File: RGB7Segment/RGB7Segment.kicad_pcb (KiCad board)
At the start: 2 copper layers, 34 x 31.5 mm, 14 parts, among them J1 Conn_01x04_Female, J2 Conn_01x04_Female

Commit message: Slotted/Cut Design Uploaded. Waiting on COnfirmation of Operation
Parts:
- removed D3, D4: SK6812-E, Library:12-23C
- removed J2: Conn_01x04_Female, Connector_PinHeader_2.54mm:PinHeader_1x04_P2.54mm_Vertical
- removed R1, R2: 0, Resistor_SMD:R_0402_1005Metric
- added A2: SK6812-E, Library:12-23C, F.Cu at (192.7, 76.5)
- added B2: SK6812-E, Library:12-23C, F.Cu at (196.7, 77.7)
- added C2: 0.470u, Capacitor_SMD:C_0402_1005Metric, F.Cu at (187.5, 77.0)
- added C3: 0.1u, Capacitor_SMD:C_0402_1005Metric, F.Cu at (181.2, 78.8)
- added C4: 0.1u, Capacitor_SMD:C_0402_1005Metric, F.Cu at (181.5, 85.0)
- added C5: SK6812-E, Library:12-23C, F.Cu at (196.7, 83.7)
- added C8: 0.1u, Capacitor_SMD:C_0402_1005Metric, F.Cu at (194.2, 79.0)
- added C9: 0.1u, Capacitor_SMD:C_0402_1005Metric, F.Cu at (193.9, 85.2)
- added E2: SK6812-E, Library:12-23C, F.Cu at (191.4, 86.3)
- added F2: SK6812-E, Library:12-23C, F.Cu at (191.4, 80.3)
- added G2: SK6812-E, Library:12-23C, F.Cu at (192.7, 82.5)
- A1, D1: footprint Library:4960_ADA -> Library:12-23C
- B1: footprint Library:4960_Test2 -> Library:12-23C
- C1, G1: footprint Library:4960_Test4 -> Library:12-23C
- E1: footprint Library:4960_Test3 -> Library:12-23C
- F1: footprint Library:4960_Test1 -> Library:12-23C
- moved C1 27.0 mm to (184.0, 83.7), turned to -90 degrees
- moved D2 26.1 mm to (195.3, 87.5), turned to 180 degrees
- moved B1 25.1 mm to (184.0, 77.7), turned to -90 degrees
- moved D1 24.1 mm to (182.6, 87.5), turned to 180 degrees
- moved G1 24.0 mm to (180.0, 82.5), turned to 0 degrees
- moved A1 22.1 mm to (180.0, 76.5)
- moved E1 21.0 mm to (178.7, 86.3), turned to 90 degrees
- moved F1 19.0 mm to (178.7, 80.3), turned to 90 degrees
- moved J1 8.30 mm to (187.5, 80.0)
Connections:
- net +3V3 renamed VCC
- A1 pad 2: Net-(A1-Pad2) -> /F1
- A1 pad 4: Net-(R2-Pad2) -> /A1
- B1 pad 2: Net-(B1-Pad2) -> /A1
- B1 pad 4: Net-(A1-Pad2) -> /DIN
- C1 pad 2: /D1 -> /G1
- C1 pad 4: Net-(B1-Pad2) -> /C1
- D1 pad 2: Net-(D1-Pad2) -> /C1
- D2 pad 2: Net-(D2-Pad2) -> /C2
- D2 pad 4: Net-(D2-Pad4) -> /D2
- E1 pad 2: Net-(E1-Pad2) -> /D1
- E1 pad 4: Net-(D1-Pad2) -> /E1
- F1 pad 2: Net-(F1-Pad2) -> /E1
- F1 pad 4: Net-(E1-Pad2) -> /F1
- G1 pad 2: /D2 -> /E2
- G1 pad 4: Net-(F1-Pad2) -> /G1
- J1 pad 3: unconnected-(J1-Pad3) -> /DOUT
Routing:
- net VCC: track 130.3 -> 68.7 mm, vias 0 -> 4
- net Net-(E1-Pad2): track 21.2 -> 0.00 mm
- net /DIN: track 24.8 -> 5.04 mm
- net Net-(D2-Pad4): track 18.3 -> 0.00 mm
- net /E2: track 0.00 -> 16.1 mm
- net Net-(A1-Pad2): track 12.6 -> 0.00 mm
- net Net-(R2-Pad2): track 12.0 -> 0.00 mm
- net Net-(B1-Pad2): track 11.0 -> 0.00 mm
- net Net-(F1-Pad2): track 9.52 -> 0.00 mm
- net Net-(D2-Pad2): track 8.73 -> 0.00 mm
- net Net-(D1-Pad2): track 8.00 -> 0.00 mm
- net /DOUT: track 0.00 -> 7.65 mm, vias 0 -> 1
- net /G2: track 0.00 -> 7.44 mm, vias 0 -> 2
- net GND: track 13.8 -> 18.6 mm, vias 9 -> 19
- net /B2: track 0.00 -> 3.67 mm
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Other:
- board size 34 x 31.5 mm -> 21.8 x 14.5 mm

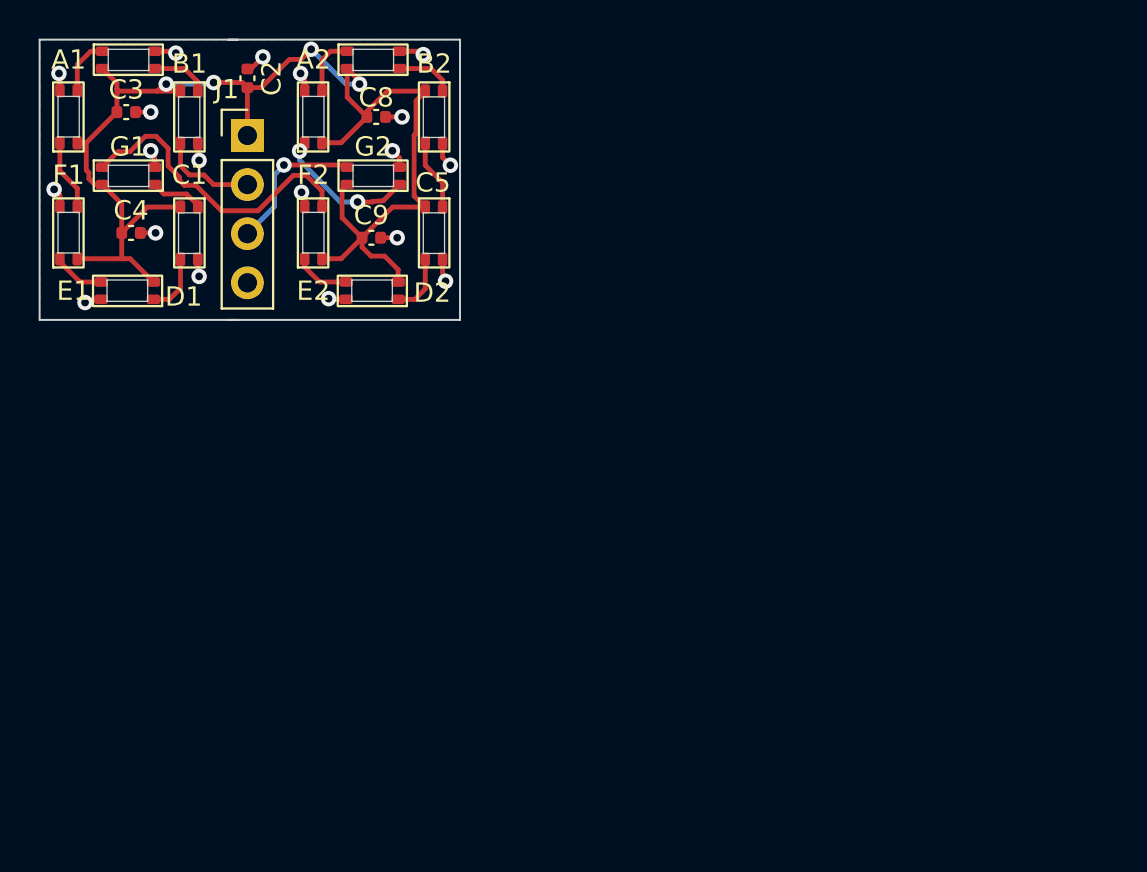
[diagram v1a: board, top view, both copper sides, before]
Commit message: Moving Design over to non cutout.
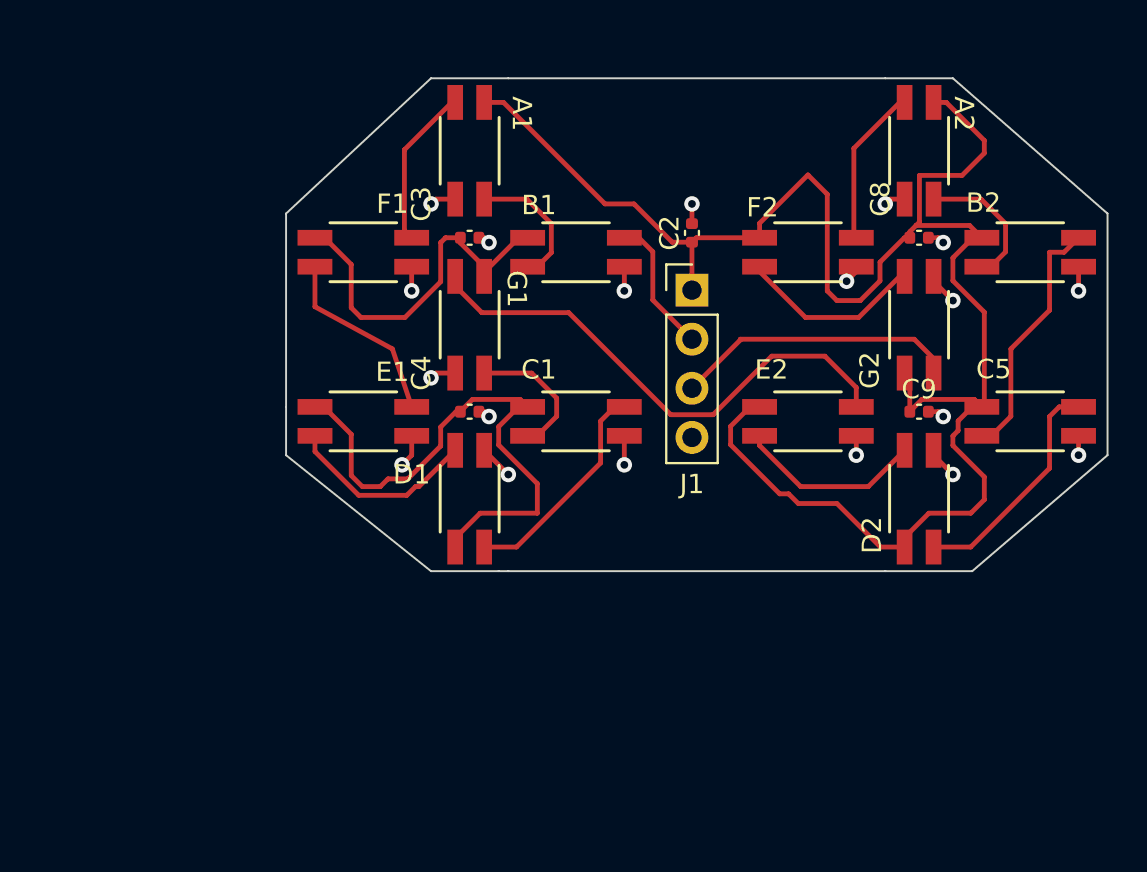
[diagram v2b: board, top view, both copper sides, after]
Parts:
- A1, A2, B1, B2, C1, C5, D1, D2, E1, E2, F1, F2, G1, G2: footprint Library:12-23C -> Library:4960_Test4
- moved C5 33.2 mm to (228.0, 94.7), turned to 0 degrees
- moved B2 32.4 mm to (228.0, 86.0), turned to 0 degrees
- moved G2 30.5 mm to (222.3, 89.8), turned to 90 degrees
- moved A2 29.9 mm to (222.3, 80.8), turned to -90 degrees
- moved C9 29.7 mm to (222.3, 94.3)
- moved D2 29.2 mm to (222.3, 98.8), turned to 90 degrees
- moved C8 28.8 mm to (222.3, 85.3)
- moved E2 26.5 mm to (216.5, 94.8), turned to 0 degrees
- moved F2 25.8 mm to (216.5, 86.0), turned to 0 degrees
- moved C2 24.4 mm to (210.5, 85.0)
- moved J1 24.4 mm to (210.5, 88.0)
- moved C1 23.3 mm to (204.5, 94.8), turned to 0 degrees
- moved B1 22.1 mm to (204.5, 86.0), turned to 0 degrees
- moved G1 20.3 mm to (199.0, 89.8), turned to -90 degrees
- moved D1 19.8 mm to (199.0, 98.8), turned to 90 degrees
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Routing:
- net VCC: track 68.7 -> 142.6 mm, vias 4 -> 0
- net /E2: track 16.1 -> 26.9 mm
- net /B2: track 3.67 -> 13.1 mm
- net /C2: track 3.16 -> 12.1 mm
- net /C1: track 3.14 -> 11.5 mm
- net /D1: track 2.73 -> 9.97 mm
- net /DOUT: track 7.65 -> 14.7 mm, vias 1 -> 0
- net /D2: track 2.88 -> 9.66 mm
- net /E1: track 3.67 -> 9.79 mm
- net /F1: track 2.93 -> 8.35 mm
- net /F2: track 3.08 -> 8.29 mm
- net GND: track 18.6 -> 22.8 mm
- net /A2: track 3.05 -> 7.26 mm
- net /G1: track 2.99 -> 7.15 mm
- net /A1: track 3.00 -> 7.03 mm
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- removed copper zone on B.Cu, net GND
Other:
- board size 21.8 x 14.5 mm -> 42.5 x 25.5 mm

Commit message: Cleaning up PCB, and minor cleanup.
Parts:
- added J2: Conn_01x02_Socket, Connector_PinHeader_2.54mm:PinHeader_1x02_P2.54mm_Vertical, F.Cu at (207.2, 100.0)
- J1: value Conn_01x04_Female -> Conn_01x02_Socket; footprint Connector_PinHeader_2.54mm:PinHeader_1x04_P2.54mm_Vertical -> Connector_PinHeader_2.54mm:PinHeader_1x02_P2.54mm_Vertical
- moved J1 9.07 mm to (207.2, 79.5), turned to 90 degrees
- moved A2 4.00 mm to (218.3, 80.8)
- moved B2 4.00 mm to (224.0, 86.0)
- moved C5 4.00 mm to (224.0, 94.7)
- moved C8 4.00 mm to (218.3, 85.3)
- moved C9 4.00 mm to (218.3, 94.3)
- moved D2 4.00 mm to (218.3, 98.8)
- moved E2 4.00 mm to (212.5, 94.8)
- moved F2 4.00 mm to (212.5, 86.0)
- moved G2 4.00 mm to (218.3, 89.8)
- moved C2 3.61 mm to (208.5, 82.0), turned to 180 degrees
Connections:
- J1 pad 1: VCC -> GND
- J1 pad 2: /DIN -> VCC
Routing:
- net VCC: track 142.6 -> 3.70 mm
- net /E2: track 26.9 -> 0.00 mm
- net GND: track 22.8 -> 1.02 mm, vias 19 -> 1
- net /DOUT: track 14.7 -> 0.00 mm
- net /B2: track 13.1 -> 0.00 mm
- net /C2: track 12.1 -> 0.00 mm
- net /C1: track 11.5 -> 0.00 mm
- net /D1: track 9.97 -> 0.00 mm
- net /E1: track 9.79 -> 0.00 mm
- net /D2: track 9.66 -> 0.00 mm
- net /G2: track 9.62 -> 0.00 mm
- net /F1: track 8.35 -> 0.00 mm
- net /F2: track 8.29 -> 0.00 mm
- net /A2: track 7.26 -> 0.00 mm
- net /G1: track 7.15 -> 0.00 mm
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- added copper zone on B.Cu, net GND
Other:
- board size 42.5 x 25.5 mm -> 38.5 x 25.5 mm

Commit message: Adding New Models,
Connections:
- A1 pad 2: /F1 -> unconnected-(A1-DOUT-Pad2)
- A1 pad 4: /A1 -> unconnected-(A1-DIN-Pad4)
- A2 pad 2: /F2 -> unconnected-(A2-DOUT-Pad2)
- A2 pad 4: /A2 -> unconnected-(A2-DIN-Pad4)
- B1 pad 2: /A1 -> unconnected-(B1-DOUT-Pad2)
- B1 pad 4: /DIN -> unconnected-(B1-DIN-Pad4)
- B2 pad 2: /A2 -> unconnected-(B2-DOUT-Pad2)
- B2 pad 4: /B2 -> unconnected-(B2-DIN-Pad4)
- C1 pad 2: /G1 -> unconnected-(C1-DOUT-Pad2)
- C1 pad 4: /C1 -> /DIN
- C5 pad 2: /B2 -> unconnected-(C5-DOUT-Pad2)
- C5 pad 4: /C2 -> unconnected-(C5-DIN-Pad4)
- D1 pad 2: /C1 -> unconnected-(D1-DOUT-Pad2)
- D1 pad 4: /D1 -> unconnected-(D1-DIN-Pad4)
- D2 pad 2: /C2 -> unconnected-(D2-DOUT-Pad2)
- D2 pad 4: /D2 -> unconnected-(D2-DIN-Pad4)
- E1 pad 2: /D1 -> unconnected-(E1-DOUT-Pad2)
- E1 pad 4: /E1 -> unconnected-(E1-DIN-Pad4)
- E2 pad 2: /D2 -> /DOUT
- E2 pad 4: /E2 -> unconnected-(E2-DIN-Pad4)
- F1 pad 2: /E1 -> unconnected-(F1-DOUT-Pad2)
- F1 pad 4: /F1 -> unconnected-(F1-DIN-Pad4)
- F2 pad 2: /G2 -> unconnected-(F2-DOUT-Pad2)
- F2 pad 4: /F2 -> unconnected-(F2-DIN-Pad4)
- G1 pad 2: /E2 -> unconnected-(G1-DOUT-Pad2)
- G1 pad 4: /G1 -> unconnected-(G1-DIN-Pad4)
- G2 pad 2: /DOUT -> unconnected-(G2-DOUT-Pad2)
- G2 pad 4: /G2 -> unconnected-(G2-DIN-Pad4)
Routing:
- net VCC: track 3.70 -> 0.88 mm
- net GND: track 1.02 -> 0.00 mm, vias 1 -> 0

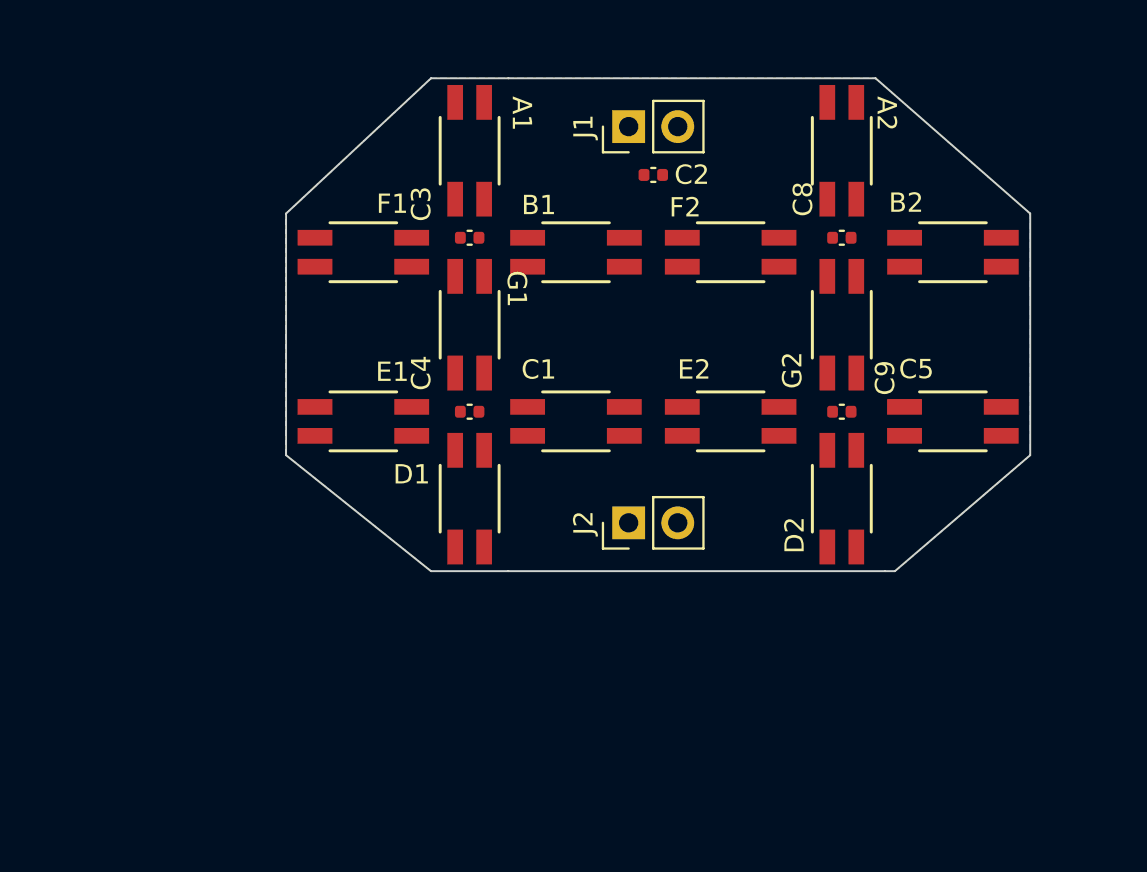
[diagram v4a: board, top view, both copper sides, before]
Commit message: Smaller Size first pass layout
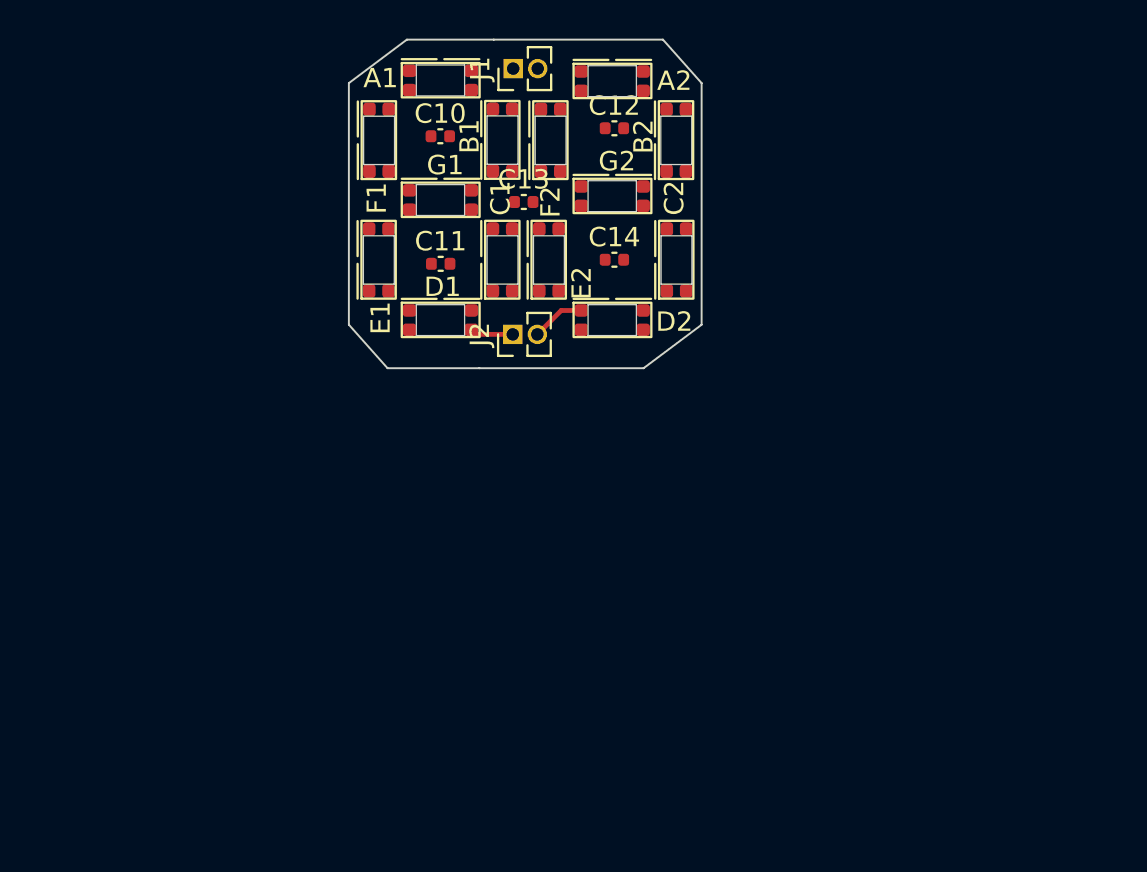
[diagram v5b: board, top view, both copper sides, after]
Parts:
- removed C3, C4, C8, C9: 0.1u, Capacitor_SMD:C_0402_1005Metric
- removed C5: SK6812-E, Library:4960_Test4
- added C10: 0.1u, Capacitor_SMD:C_0402_1005Metric, F.Cu at (197.5, 80.0)
- added C11: 0.1u, Capacitor_SMD:C_0402_1005Metric, F.Cu at (197.5, 86.6)
- added C12: 0.1u, Capacitor_SMD:C_0402_1005Metric, F.Cu at (206.5, 79.6)
- added C13: 0.470u, Capacitor_SMD:C_0402_1005Metric, F.Cu at (201.8, 83.4)
- added C14: 0.1u, Capacitor_SMD:C_0402_1005Metric, F.Cu at (206.5, 86.4)
- A1, A2, B1, B2, C1, D1, D2, E1, E2, F1, F2, G1, G2: footprint Library:4960_Test4 -> Library:12-23C
- C2: value 0.470u -> SK6812-E; footprint Capacitor_SMD:C_0402_1005Metric -> Library:12-23C
- J1, J2: footprint Connector_PinHeader_2.54mm:PinHeader_1x02_P2.54mm_Vertical -> Connector_PinHeader_1.27mm:PinHeader_1x02_P1.27mm_Vertical
- moved D2 15.9 mm to (205.0, 90.0), turned to 0 degrees
- moved G2 14.6 mm to (205.0, 83.5), turned to 0 degrees
- moved B2 14.6 mm to (210.1, 81.6), turned to 90 degrees
- moved A2 13.6 mm to (205.0, 77.6), turned to 0 degrees
- moved J2 11.4 mm to (201.2, 90.2)
- moved E2 11.4 mm to (203.6, 87.8), turned to 90 degrees
- moved F2 9.91 mm to (203.6, 81.6), turned to 90 degrees
- moved D1 9.24 mm to (196.1, 90.0), turned to 0 degrees
- moved C1 7.76 mm to (201.1, 87.8), turned to 90 degrees
- moved E1 7.11 mm to (194.8, 87.8), turned to 90 degrees
- moved J1 6.69 mm to (201.2, 76.5)
- moved G1 6.65 mm to (196.1, 83.8), turned to 0 degrees
- moved C2 5.98 mm to (210.2, 87.8), turned to 90 degrees
- moved B1 5.57 mm to (201.1, 81.5), turned to 90 degrees
- moved F1 4.61 mm to (194.8, 81.6), turned to 90 degrees
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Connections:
- C1 pad 4: /DIN -> unconnected-(C1-DIN-Pad4)
- C2 pad 2: GND -> unconnected-(C2-DOUT-Pad2)
- D1 pad 4: unconnected-(D1-DIN-Pad4) -> /DIN
- D2 pad 2: unconnected-(D2-DOUT-Pad2) -> /DOUT
- E2 pad 2: /DOUT -> unconnected-(E2-DOUT-Pad2)
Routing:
- net /DOUT: track 0.00 -> 2.79 mm
- net /DIN: track 0.00 -> 2.24 mm
- net VCC: track 0.88 -> 0.00 mm
- removed copper zone on B.Cu, net GND
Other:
- board size 38.5 x 25.5 mm -> 18.2 x 17 mm

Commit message: New Pass of RGB 7 Segment
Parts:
- moved F1 3.12 mm to (193.7, 78.6), turned to -90 degrees
- moved F2 3.06 mm to (202.7, 78.6), turned to -90 degrees
- moved E1 3.05 mm to (193.7, 84.9), turned to -90 degrees
- moved A1 2.95 mm to (198.9, 76.4), turned to 180 degrees
- moved A2 2.84 mm to (207.6, 76.4), turned to 180 degrees
- moved E2 2.83 mm to (202.7, 85.0), turned to -90 degrees
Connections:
- A1 pad 2: unconnected-(A1-DOUT-Pad2) -> Net-(A1-DOUT)
- A1 pad 4: unconnected-(A1-DIN-Pad4) -> Net-(A1-DIN)
- A2 pad 2: unconnected-(A2-DOUT-Pad2) -> Net-(A2-DOUT)
- A2 pad 4: unconnected-(A2-DIN-Pad4) -> Net-(A2-DIN)
- B1 pad 2: unconnected-(B1-DOUT-Pad2) -> Net-(B1-DOUT)
- B1 pad 4: unconnected-(B1-DIN-Pad4) -> Net-(A1-DOUT)
- B2 pad 2: unconnected-(B2-DOUT-Pad2) -> Net-(B2-DOUT)
- B2 pad 4: unconnected-(B2-DIN-Pad4) -> Net-(A2-DOUT)
- C1 pad 2: unconnected-(C1-DOUT-Pad2) -> /E2
- C1 pad 4: unconnected-(C1-DIN-Pad4) -> Net-(C1-DIN)
- C2 pad 2: unconnected-(C2-DOUT-Pad2) -> Net-(C2-DOUT)
- C2 pad 4: unconnected-(C2-DIN-Pad4) -> Net-(B2-DOUT)
- D1 pad 2: unconnected-(D1-DOUT-Pad2) -> Net-(D1-DOUT)
- D2 pad 4: unconnected-(D2-DIN-Pad4) -> Net-(D2-DIN)
- E1 pad 2: unconnected-(E1-DOUT-Pad2) -> Net-(E1-DOUT)
- E1 pad 4: unconnected-(E1-DIN-Pad4) -> Net-(D1-DOUT)
- E2 pad 2: unconnected-(E2-DOUT-Pad2) -> Net-(E2-DOUT)
- E2 pad 4: unconnected-(E2-DIN-Pad4) -> /E2
- F1 pad 2: unconnected-(F1-DOUT-Pad2) -> Net-(A1-DIN)
- F1 pad 4: unconnected-(F1-DIN-Pad4) -> Net-(E1-DOUT)
- F2 pad 2: unconnected-(F2-DOUT-Pad2) -> Net-(A2-DIN)
- F2 pad 4: unconnected-(F2-DIN-Pad4) -> Net-(E2-DOUT)
- G1 pad 2: unconnected-(G1-DOUT-Pad2) -> Net-(C1-DIN)
- G1 pad 4: unconnected-(G1-DIN-Pad4) -> Net-(B1-DOUT)
- G2 pad 2: unconnected-(G2-DOUT-Pad2) -> Net-(D2-DIN)
- G2 pad 4: unconnected-(G2-DIN-Pad4) -> Net-(C2-DOUT)
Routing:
- net VCC: track 0.00 -> 109.8 mm, vias 0 -> 8
- net GND: track 0.00 -> 52.9 mm, vias 0 -> 5
- net Net-(D2-DIN): track 0.00 -> 11.1 mm, vias 0 -> 2
- net Net-(C1-DIN): track 0.00 -> 8.83 mm, vias 0 -> 2
- net Net-(C2-DOUT): track 0.00 -> 5.21 mm, vias 0 -> 2
- net /E2: track 0.00 -> 3.95 mm
- net Net-(E1-DOUT): track 0.00 -> 3.46 mm
- net Net-(E2-DOUT): track 0.00 -> 3.42 mm
- net Net-(B2-DOUT): track 0.00 -> 3.25 mm
- net Net-(A2-DOUT): track 0.00 -> 3.04 mm
- net Net-(D1-DOUT): track 0.00 -> 2.94 mm
- net Net-(A1-DOUT): track 0.00 -> 2.79 mm
- net Net-(A1-DIN): track 0.00 -> 2.73 mm
- net Net-(B1-DOUT): track 0.00 -> 2.67 mm
- net Net-(A2-DIN): track 0.00 -> 2.61 mm
- added copper zone on B.Cu, net GND
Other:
- board size 18.2 x 17 mm -> 18.3 x 17 mm
